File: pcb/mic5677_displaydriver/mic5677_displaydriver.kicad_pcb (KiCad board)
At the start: 2 copper layers, 180 x 110 mm, 81 parts, among them J1 Segment DIP14, J2 Segment DIP14, J3 Segment Wire Connector, J4 Common Cathode Enable, J5 PSU, J6 Bypass, J7 Serial Debug, J8 8P8C, Q1 D45H8G, Q10 BC546, Q11 BC546, Q12 BC546, Q13 BC546, Q14 BC546, Q15 BC546, Q16 BC546, Q17 BC546, Q18 BC546, Q19 BC546, Q2 D45H8G, Q20 BC546, Q21 BC546, Q22 BC546, Q23 BC546, Q3 D45H8G, Q4 D45H8G, Q5 D45H8G, Q6 D45H8G, Q7 D45H8G, Q8 D45H8G, Q9 D45H8G, U1 L7805, U2 74HC595, U3 74HC595, U4 74HC02

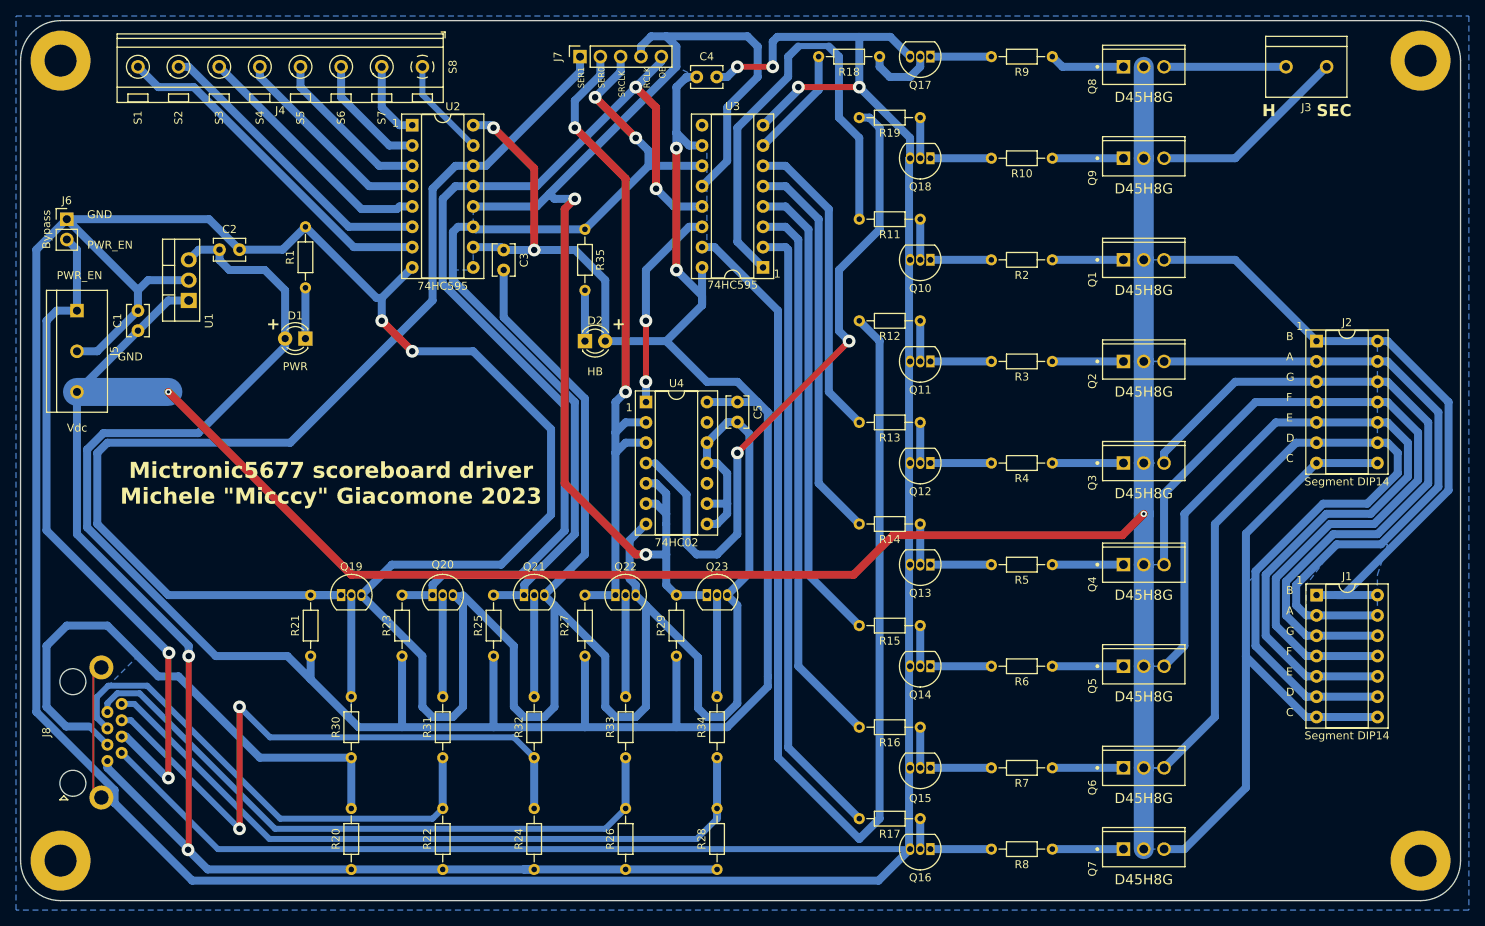
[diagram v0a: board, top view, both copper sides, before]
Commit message: Added ddriver front printable document
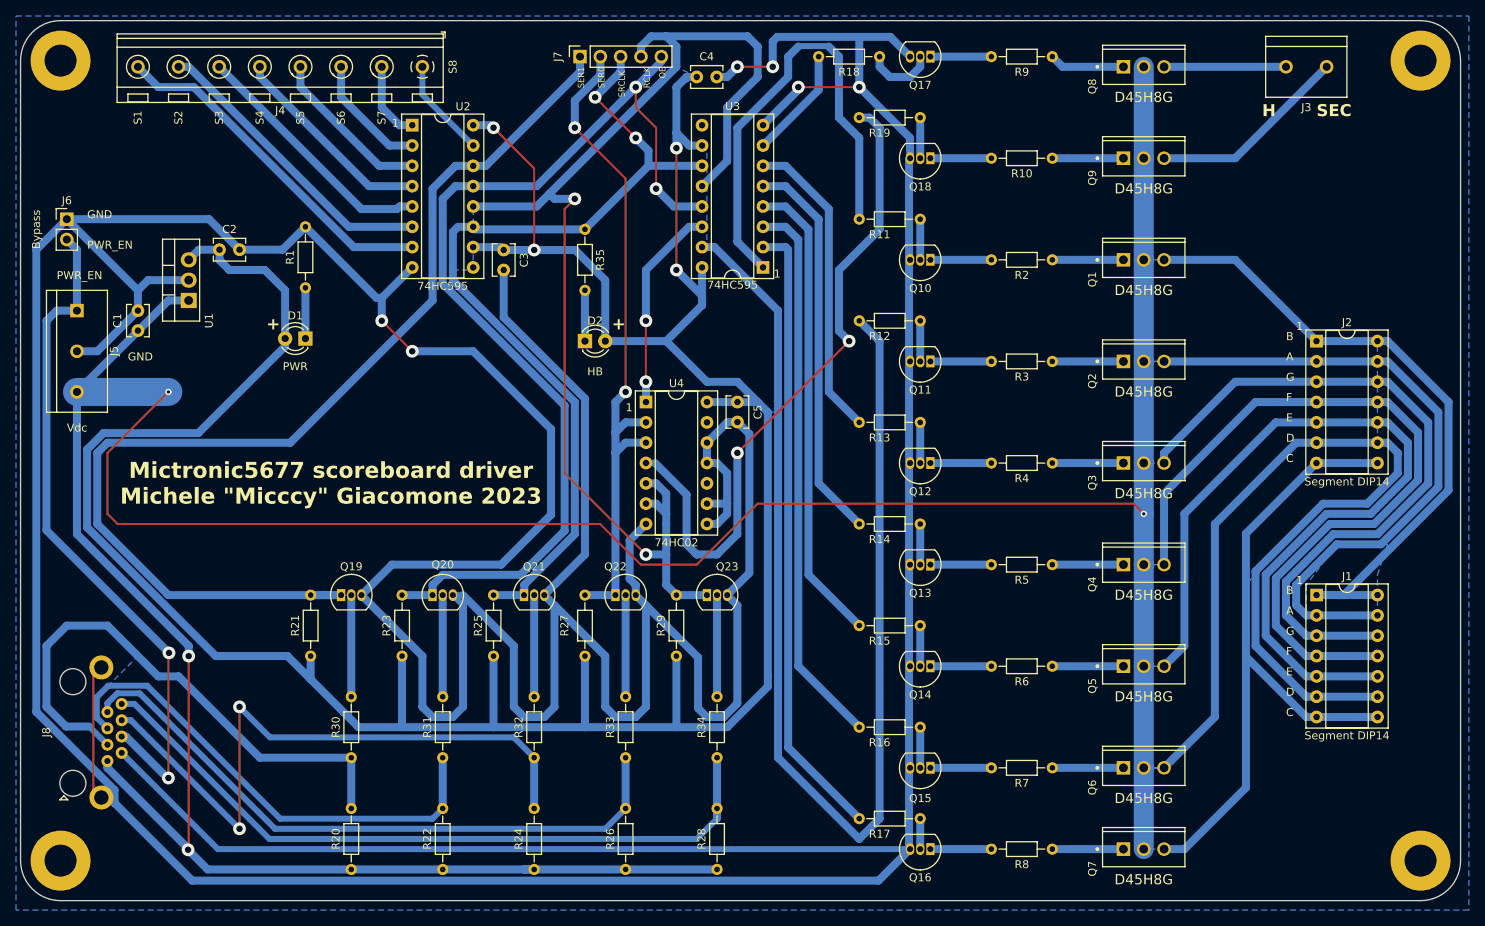
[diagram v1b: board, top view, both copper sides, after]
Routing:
- net VDC: track 409.2 -> 428.9 mm
- net RCLK: track 153.3 -> 152.5 mm

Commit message: Added power pins on serial debug port
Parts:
- J7: footprint Connector_PinSocket_2.54mm:PinSocket_1x05_P2.54mm_Vertical -> Connector_PinSocket_2.54mm:PinSocket_1x07_P2.54mm_Vertical
- moved J7 5.73 mm to (109.2, 49.5)
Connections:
- J7 pad 1: SER1 -> +5V
- J7 pad 2: SER0 -> GND
- J7 pad 3: SRCLK -> SER1
- J7 pad 4: RCLK -> SER0
- J7 pad 5: OE -> SRCLK
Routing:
- net GND: track 858.3 -> 939.4 mm
- net +5V: track 355.4 -> 367.1 mm
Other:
- board text added: "+5V"

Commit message: Updated ddriver to v2.3
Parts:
- moved R35 1.80 mm to (114.3, 69.8)
- turned Q1 to -90 degrees
- turned Q2 to -90 degrees
- turned Q3 to -90 degrees
- turned Q4 to -90 degrees
- turned Q5 to -90 degrees
- turned Q6 to -90 degrees
- turned Q7 to -90 degrees
- turned Q8 to -90 degrees
- turned Q9 to -90 degrees
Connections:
- Q1 pad 2: VDC -> /B_OUT
- Q1 pad 3: /B_OUT -> VDC
- Q2 pad 2: VDC -> /A_OUT
- Q2 pad 3: /A_OUT -> VDC
- Q3 pad 2: VDC -> /G_OUT
- Q3 pad 3: /G_OUT -> VDC
- Q4 pad 2: VDC -> /F_OUT
- Q4 pad 3: /F_OUT -> VDC
- Q5 pad 2: VDC -> /E_OUT
- Q5 pad 3: /E_OUT -> VDC
- Q6 pad 2: VDC -> /D_OUT
- Q6 pad 3: /D_OUT -> VDC
- Q7 pad 2: VDC -> /C_OUT
- Q7 pad 3: /C_OUT -> VDC
- Q8 pad 2: VDC -> /H_OUT
- Q8 pad 3: /H_OUT -> VDC
- Q9 pad 2: VDC -> /SEC_OUT
- Q9 pad 3: /SEC_OUT -> VDC
- R35 pad 1: SRCLK -> RCLK
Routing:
- net Net-(Q3-B): track 8.89 -> 21.2 mm, vias 0 -> 2
- net GND: track 939.4 -> 950.1 mm
- net Net-(Q9-B): track 8.89 -> 17.6 mm, vias 0 -> 2
- net Net-(Q5-B): track 8.89 -> 17.6 mm, vias 0 -> 2
- net Net-(Q4-B): track 8.89 -> 17.6 mm, vias 0 -> 2
- net Net-(Q1-B): track 8.89 -> 17.6 mm, vias 0 -> 2
- net Net-(Q6-B): track 8.89 -> 17.6 mm, vias 0 -> 2
- net Net-(Q2-B): track 8.89 -> 17.6 mm, vias 0 -> 2
- net Net-(Q7-B): track 8.89 -> 16.8 mm
- net Net-(Q8-B): track 9.42 -> 16.3 mm
- net /A_OUT: track 82.3 -> 87.7 mm
- net /H_OUT: track 15.2 -> 20.6 mm
- net /SEC_OUT: track 25.1 -> 30.4 mm
- net /B_OUT: track 81.0 -> 84.2 mm
- net RCLK: track 152.5 -> 155.1 mm
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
